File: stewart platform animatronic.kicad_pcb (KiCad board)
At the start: 2 copper layers, 63.5 x 53.3 mm, 23 parts, among them P1 CONN_01X03, P10 CONN_01X03, P11 CONN_01X03, P12 CONN_01X03, P13 CONN_01X02, P14 CONN_01X03, P15 CONN_01X03, P16 CONN_01X03, P17 CONN_01X03, P18 CONN_01X03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

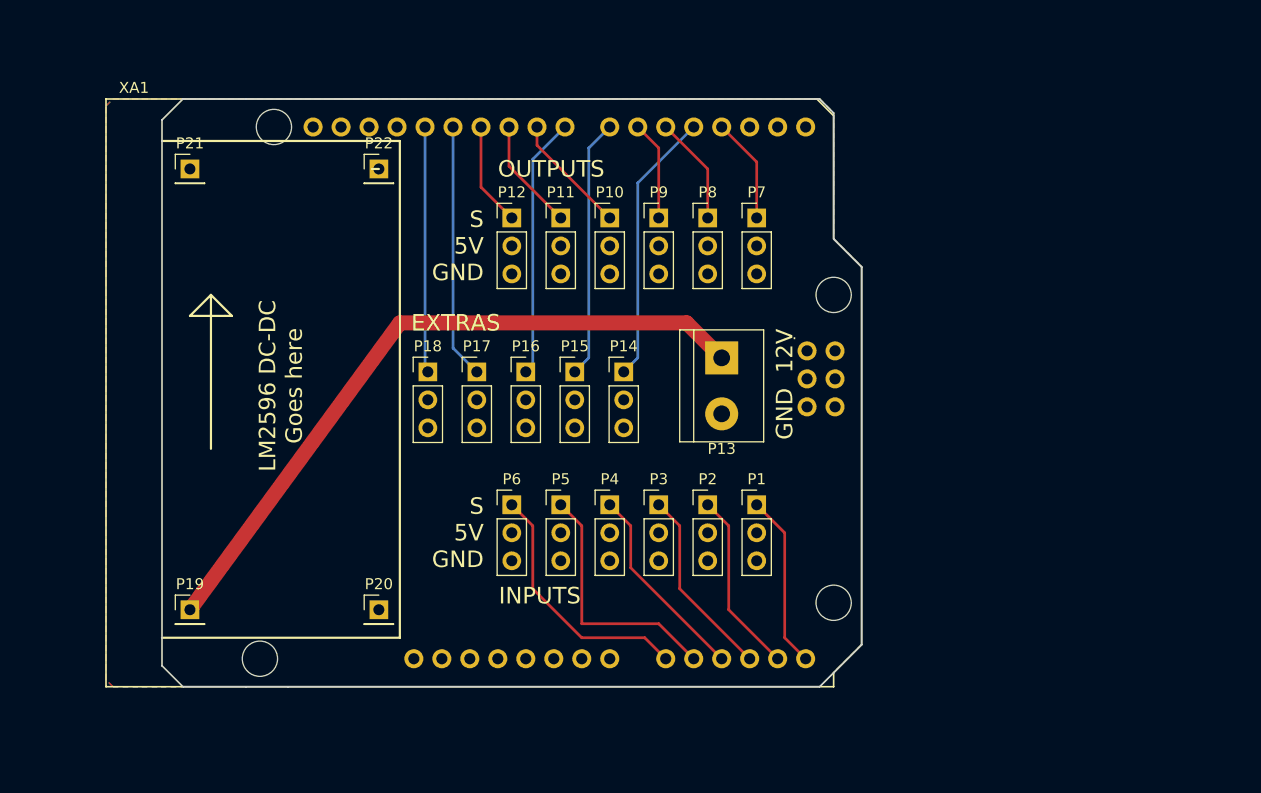
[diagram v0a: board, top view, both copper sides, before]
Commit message: updated PCB for MEGA
for MEGA design
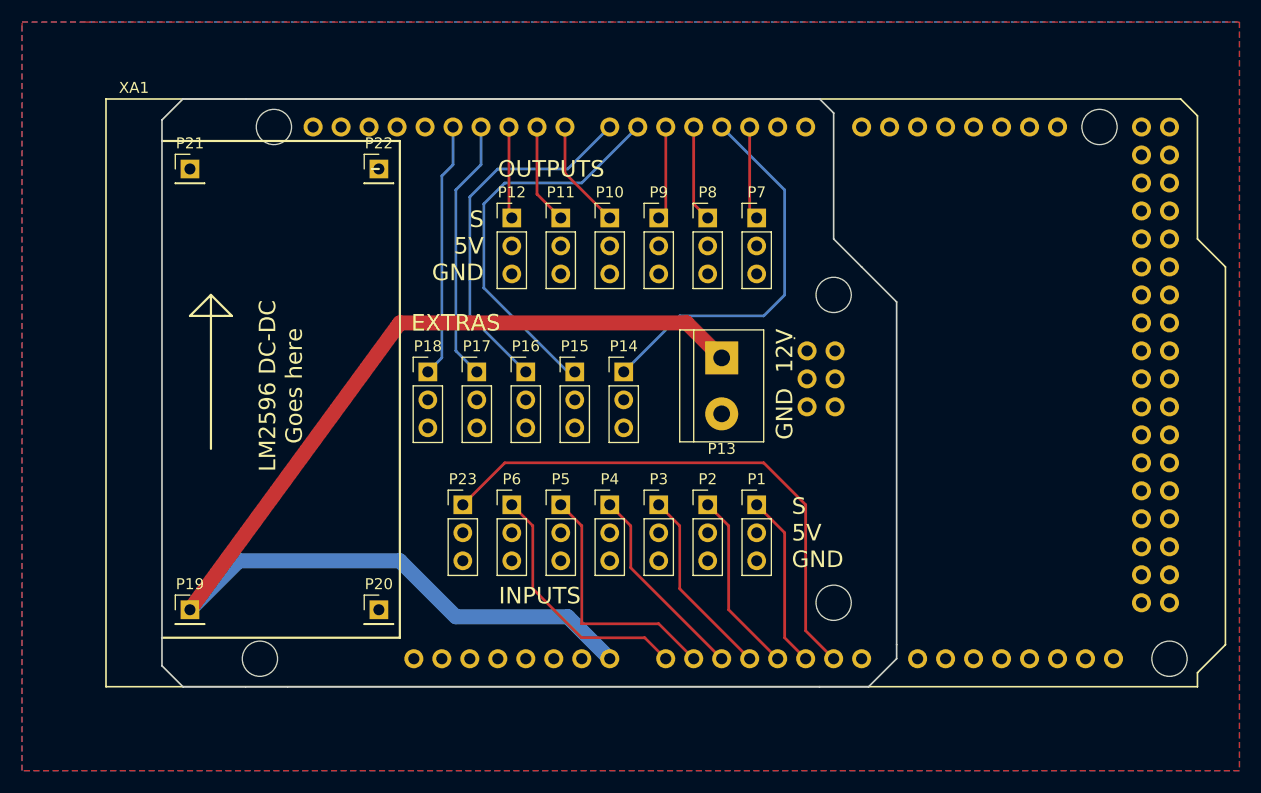
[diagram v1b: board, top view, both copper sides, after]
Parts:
- added P23: CONN_01X03, Socket_Strips:Socket_Strip_Straight_1x03_Pitch2.54mm, F.Cu at (149.9, 102.2)
- XA1: value Arduino_Uno_Shield -> Arduino_Mega2560_Shield; footprint Arduino:Arduino_Uno_Shield -> Arduino:Arduino_Mega2560_Shield
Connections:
- XA1 pad D10: Net-(P11-Pad1) -> Net-(P12-Pad1)
- XA1 pad D11: Net-(P12-Pad1) -> Net-(P17-Pad1)
- XA1 pad D12: Net-(P17-Pad1) -> Net-(P18-Pad1)
- XA1 pad D13: Net-(P18-Pad1) -> (no net)
- XA1 pad D2: (no net) -> Net-(P7-Pad1)
- XA1 pad D3: Net-(P7-Pad1) -> Net-(P14-Pad1)
- XA1 pad D4: Net-(P14-Pad1) -> Net-(P8-Pad1)
- XA1 pad D5: Net-(P8-Pad1) -> Net-(P9-Pad1)
- XA1 pad D6: Net-(P9-Pad1) -> Net-(P15-Pad1)
- XA1 pad D7: Net-(P15-Pad1) -> Net-(P16-Pad1)
- XA1 pad D8: Net-(P16-Pad1) -> Net-(P10-Pad1)
- XA1 pad D9: Net-(P10-Pad1) -> Net-(P11-Pad1)
- XA1 pad VIN: (no net) -> +12V
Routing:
- net Net-(P23-Pad1): track 0.00 -> 49.3 mm
- net +12V: track 62.8 -> 106.4 mm
- net Net-(P15-Pad1): track 23.5 -> 35.9 mm
- net Net-(P14-Pad1): track 24.9 -> 35.1 mm
- net Net-(P16-Pad1): track 24.2 -> 34.2 mm
- net Net-(P18-Pad1): track 22.7 -> 24.4 mm
- net Net-(P11-Pad1): track 10.2 -> 9.15 mm
- net Net-(P7-Pad1): track 9.57 -> 8.52 mm
- net Net-(P12-Pad1): track 9.41 -> 8.36 mm
- net Net-(P8-Pad1): track 9.83 -> 8.78 mm
- net Net-(P9-Pad1): track 9.04 -> 8.52 mm
- net Net-(P10-Pad1): track 11.0 -> 10.5 mm
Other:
- board size 63.5 x 53.3 mm -> 66.7 x 53.3 mm
- board text added: "ELEC-0132 Stewart Platform Shield v4 2018-07-30 Marginallyclever.com"
- board text removed: "ELEC-0132 Stewart Platform Shield v3 2018-07-24 Marginallyclever.com"
